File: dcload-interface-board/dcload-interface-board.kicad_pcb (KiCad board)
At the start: 4 copper layers, 48 x 68 mm, 65 parts, among them J1 Conn_02x06_Odd_Even, J200 SWD, J201 UART, SW500 KLS TS6604B, SW501 KLS TS6604B, SW502 KLS TS6604B, SW503 KLS TS6604B, SW504 KLS TS6604B, SW505 KLS TS6604B, SW506 PEC11R-4220F-S24, U100 L78L33, U200 RP2040, U201 W25Q16JV, U300 WEO012864L, Y200 12MHz

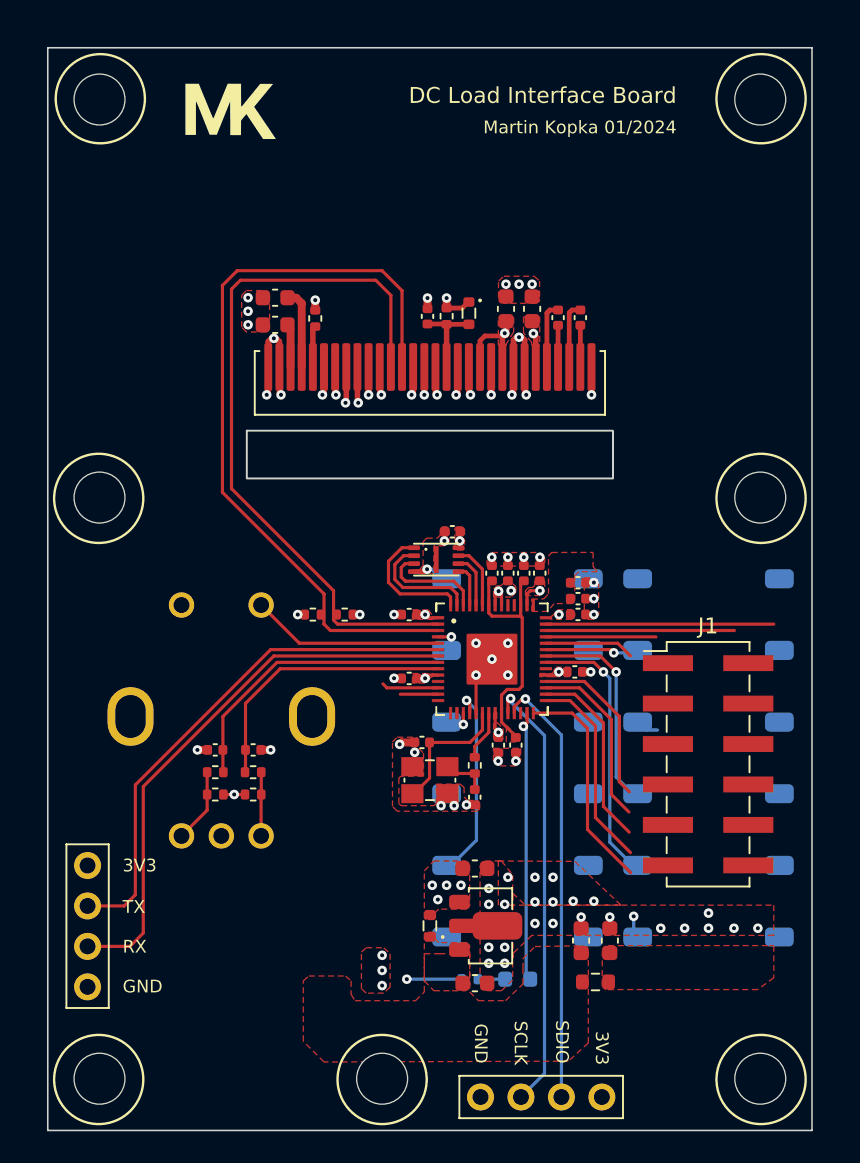
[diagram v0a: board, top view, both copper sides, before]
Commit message: add: interface panel board
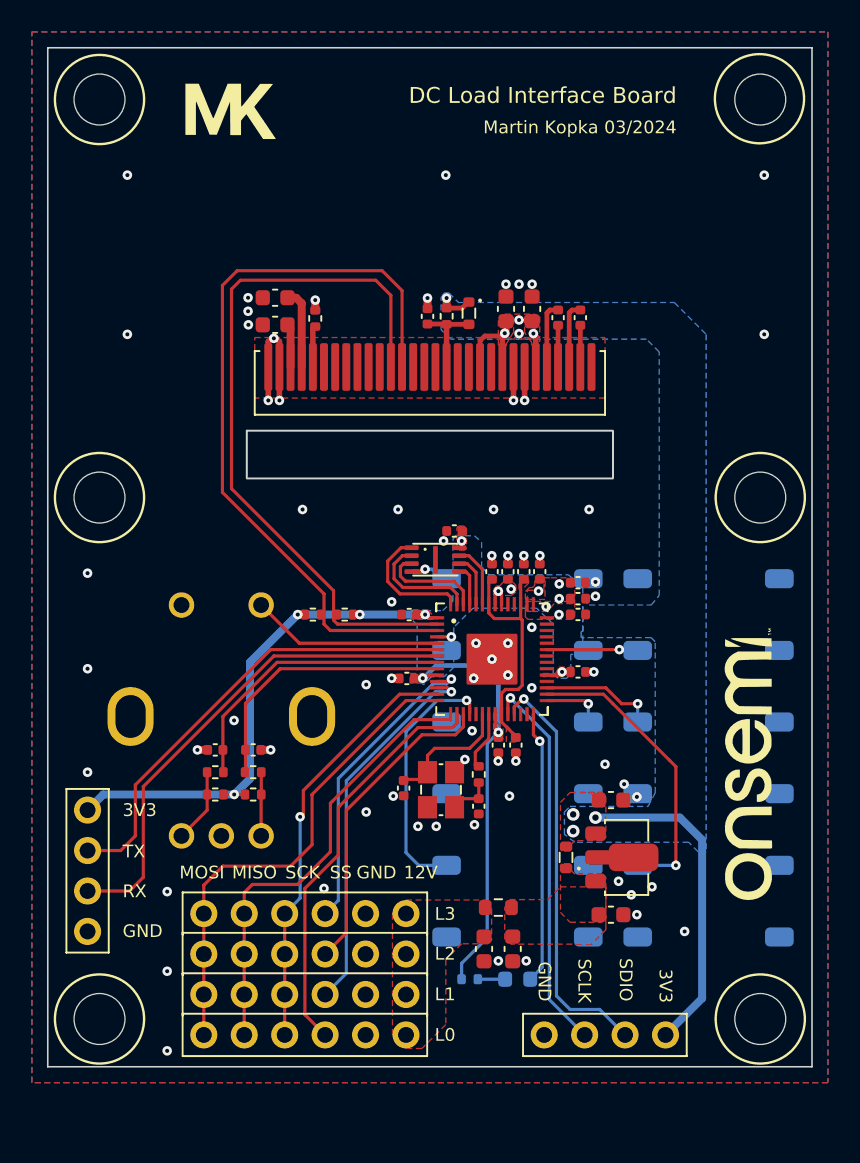
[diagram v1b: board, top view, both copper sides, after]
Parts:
- removed the H2 at (121.0, 114.8)
- removed J1: Conn_02x06_Odd_Even, Connector_PinHeader_2.54mm:PinHeader_2x06_P2.54mm_Vertical_SMD
- added G***: LOGO, LOGO, F.Cu at (144.0, 95.0)
- added J100: Conn_01x06_Male, Connector_PinHeader_2.54mm:PinHeader_1x06_P2.54mm_Vertical, F.Cu at (122.5, 112.0)
- added J101: Conn_01x06_Male, Connector_PinHeader_2.54mm:PinHeader_1x06_P2.54mm_Vertical, F.Cu at (122.5, 109.5)
- added J102: Conn_01x06_Male, Connector_PinHeader_2.54mm:PinHeader_1x06_P2.54mm_Vertical, F.Cu at (122.5, 106.9)
- added J103: Conn_01x06_Male, Connector_PinHeader_2.54mm:PinHeader_1x06_P2.54mm_Vertical, F.Cu at (122.5, 104.4)
- moved D100 9.57 mm to (132.6, 100.8)
- moved C102 9.57 mm to (135.4, 104.5)
- moved C103 9.57 mm to (135.4, 97.2)
- moved U100 9.57 mm to (136.1, 100.8)
- moved C100 7.92 mm to (127.4, 106.6), turned to -90 degrees
- moved L100 7.69 mm to (128.3, 104.0), turned to 0 degrees
- moved J200 5.59 mm to (138.8, 112.0)
- moved C101 4.33 mm to (129.2, 106.6), turned to -90 degrees
- moved H1 3.75 mm to (103.2, 111.0)
- moved H3 3.75 mm to (144.8, 111.0)
- moved J201 3.48 mm to (102.5, 97.9)
- moved C213 3.09 mm to (122.3, 96.5), turned to -90 degrees
- moved Y200 0.92 mm to (124.7, 96.6), turned to 90 degrees
- moved C212 0.62 mm to (127.1, 97.6)
- moved R200 0.62 mm to (127.1, 95.6)
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- renumbered H7 to H2
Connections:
- net /2. MCU/KEY_ISET renamed /2. MCU/KEY_SET
- net /2. MCU/KEY_OUT renamed /2. MCU/KEY_EN
- net /2. MCU/KEY_VSET renamed /2. MCU/KEY_MODE
- net Net-(C213-Pad1) renamed /2. MCU/XIN
- net Net-(R200-Pad1) renamed /2. MCU/XOUT
- C207 pad 1: +3V0 -> +3V3
- C208 pad 1: +3V0 -> +3V3
- D500 pad 1: /2. MCU/OUT_LED -> /2. MCU/EN_LED
- SW502 pad 1: /2. MCU/KEY_OVP_OCP -> /2. MCU/KEY_SEQ
- SW503 pad 1: /2. MCU/KEY_MEM -> /2. MCU/KEY_SEQ_EN
- U200 pad 11: unconnected-(U200-Pad11) -> /CMD_SS_3
- U200 pad 12: unconnected-(U200-Pad12) -> /CMD_SS_1
- U200 pad 13: unconnected-(U200-Pad13) -> /CMD_CLK
- U200 pad 14: unconnected-(U200-Pad14) -> /CMD_MOSI
- U200 pad 15: unconnected-(U200-Pad15) -> /CMD_MISO
- U200 pad 16: unconnected-(U200-Pad16) -> /CMD_SS_0
- U200 pad 17: /2. MCU/KEY_MEM -> /CMD_SS_2
- U200 pad 27: /2. MCU/OUT_LED -> unconnected-(U200-GPIO16-Pad27)
- U200 pad 28: /DAC_SS -> /2. MCU/EN_LED
- U200 pad 29: /DAC_CLK -> /2. MCU/KEY_SEQ_EN
- U200 pad 30: /DAC_MOSI -> /2. MCU/KEY_MENU
- U200 pad 31: unconnected-(U200-Pad31) -> /2. MCU/KEY_SEQ
- U200 pad 35: /2. MCU/KEY_MENU -> unconnected-(U200-GPIO23-Pad35)
- U200 pad 36: /2. MCU/KEY_OVP_OCP -> unconnected-(U200-GPIO24-Pad36)
- U200 pad 43: +3V0 -> +3V3
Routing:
- net +3V3: track 24.1 -> 95.3 mm, vias 20 -> 23
- net GND: track 55.9 -> 18.4 mm, vias 81 -> 71
- net /CMD_MOSI: track 0.00 -> 30.7 mm
- net /CMD_MISO: track 0.00 -> 28.5 mm
- net /CMD_CLK: track 0.00 -> 26.8 mm, vias 0 -> 1
- net /CMD_SS_0: track 0.00 -> 25.9 mm
- net /CMD_SS_1: track 0.00 -> 23.8 mm, vias 0 -> 1
- net /CMD_SS_2: track 0.00 -> 19.9 mm
- net /CMD_SS_3: track 0.00 -> 19.4 mm, vias 0 -> 1
- net /2. MCU/EN_LED: track 0.00 -> 17.2 mm, vias 0 -> 1
- net /2. MCU/OUT_LED: track 17.0 -> 0.00 mm, vias 1 -> 0
- net unconnected-(U200-GPIO29/ADC3-Pad41): track 14.3 -> 0.00 mm
- net /DAC_SS: track 14.0 -> 0.00 mm
- net /2. MCU/KEY_OVP_OCP: track 13.2 -> 0.00 mm, vias 1 -> 0
- net /DAC_CLK: track 12.6 -> 0.00 mm
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- added copper zone on B.Cu, net +3V3
- added copper zone on B.Cu, net GND
- removed copper zone on F.Cu, net +3V0
- removed copper zone on In2.Cu, net +3V3
- removed copper zone on In1.Cu, net GND
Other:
- board size 48 x 68 mm -> 48 x 64 mm
- copper layers 4 -> 2
- board text added: "12V"
- board text added: "EN"
- board text added: "L0"
- board text added: "L1"
- board text added: "L2"
- board text added: "L3"
- board text added: "MENU"
- board text added: "MISO"
- board text added: "MODE"
- board text added: "MOSI"
- board text added: "Martin Kopka 03/2024"
- board text added: "SCK"
- board text added: "SEQ"
- board text added: "SEQ_EN"
- board text added: "SET"
- board text added: "SS"
- board text removed: "Martin Kopka 01/2024"
- board text removed: "PCB"
